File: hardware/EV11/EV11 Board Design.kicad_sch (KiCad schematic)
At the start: 141 parts, among them CN2 Conn_05x02_Female, CN3 Conn_01x06_Female, CN4 Conn_01x06_Female, CN5 Conn_02x05_Male, CN6 Conn_02x05_Male, CN7 Conn_02x05_Male, J1 Conn_01x02_Socket, J10 Conn_01x08_Socket, J2 AudioJack1, J3 Conn_01x06_Socket, J9 USB_C_Receptacle, SW1 TS-1037-A11B3-D2, SW3 TS-1037-A11B3-D2, SW4 SW_Push, SW5 SW_Push, SW6 SW_SPDT, U1 STM32F405RGTx, U11 ESP32-S3-WROOM-1-N8R2, U13 BM14B(0.8)-24DS-0.4V(53), U2 BQ21040DBV, U3 CH340C, U4 USBLC6-2P6, U5 M24C02-RMN6TP, U6 WM8960CGEFL/RV, U7 TPS63060, U8 STM32F070CBTx, U9 WM8960CGEFL/RV, Y1 Crystal_GND24

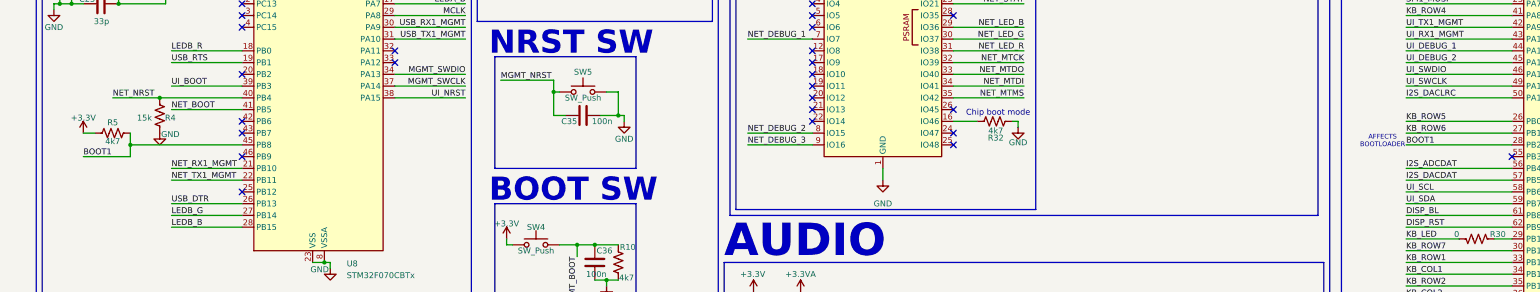
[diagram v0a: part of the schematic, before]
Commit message: Added larger courtyard to the keyboard connector to match the physical connector
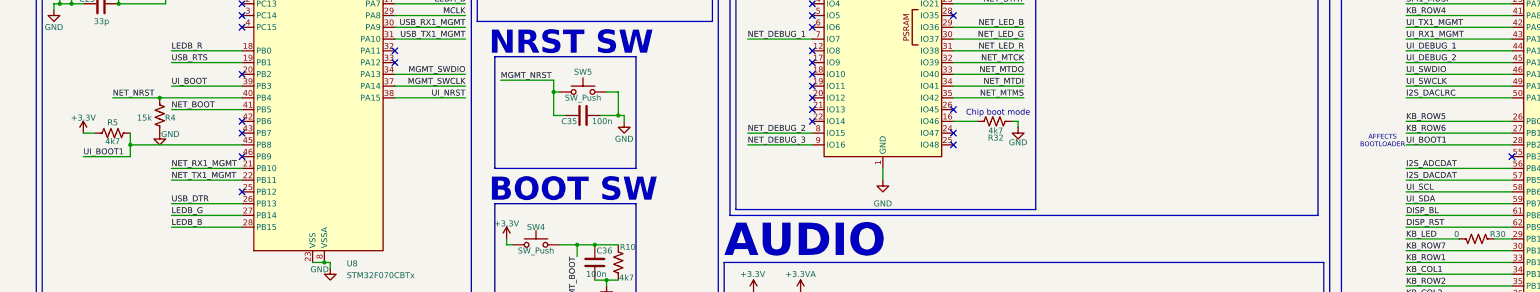
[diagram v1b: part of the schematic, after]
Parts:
- U13: footprint BM14B(0.B)-24DS-0:BM14B(0.B)-24DS-0.4V(53) -> Hactar_Footprints:BM14B(0.B)-24DS-0.4V(53)
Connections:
- net BOOT1 renamed UI_BOOT1
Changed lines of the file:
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@@
 		)
 	)
-	(label "BOOT1"
+	(label "UI_BOOT1"
 		(at 325.12 142.24 0)
 		(fields_autoplaced yes)
@@
 		)
 	)
-	(label "BOOT1"
+	(label "UI_BOOT1"
 		(at 39.37 144.78 0)
 		(fields_autoplaced yes)
@@
 			)
 		)
-		(property "Footprint" "BM14B(0.B)-24DS-0:BM14B(0.B)-24DS-0.4V(53)"
+		(property "Footprint" "Hactar_Footprints:BM14B(0.B)-24DS-0.4V(53)"
 			(at 355.6 306.07 0)
 			(effects

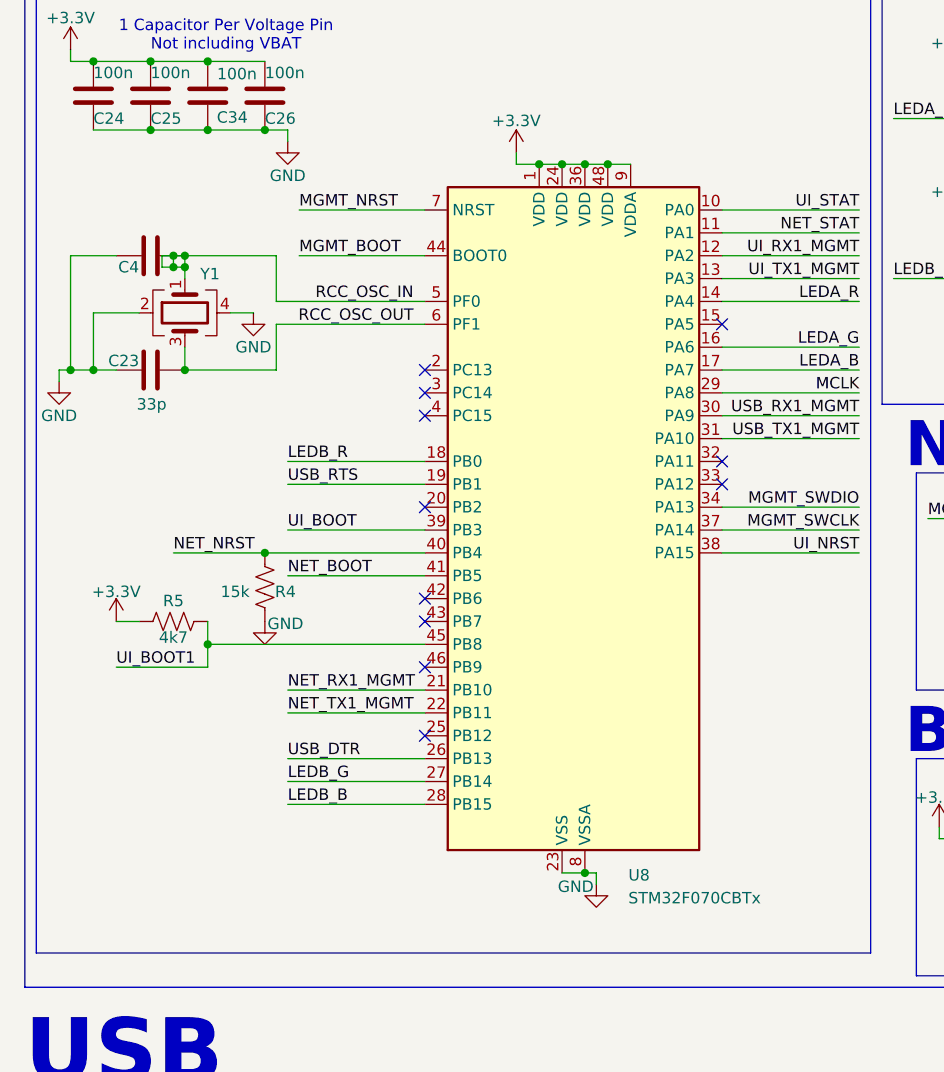
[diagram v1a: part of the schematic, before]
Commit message: Fix jlcpcb attributes
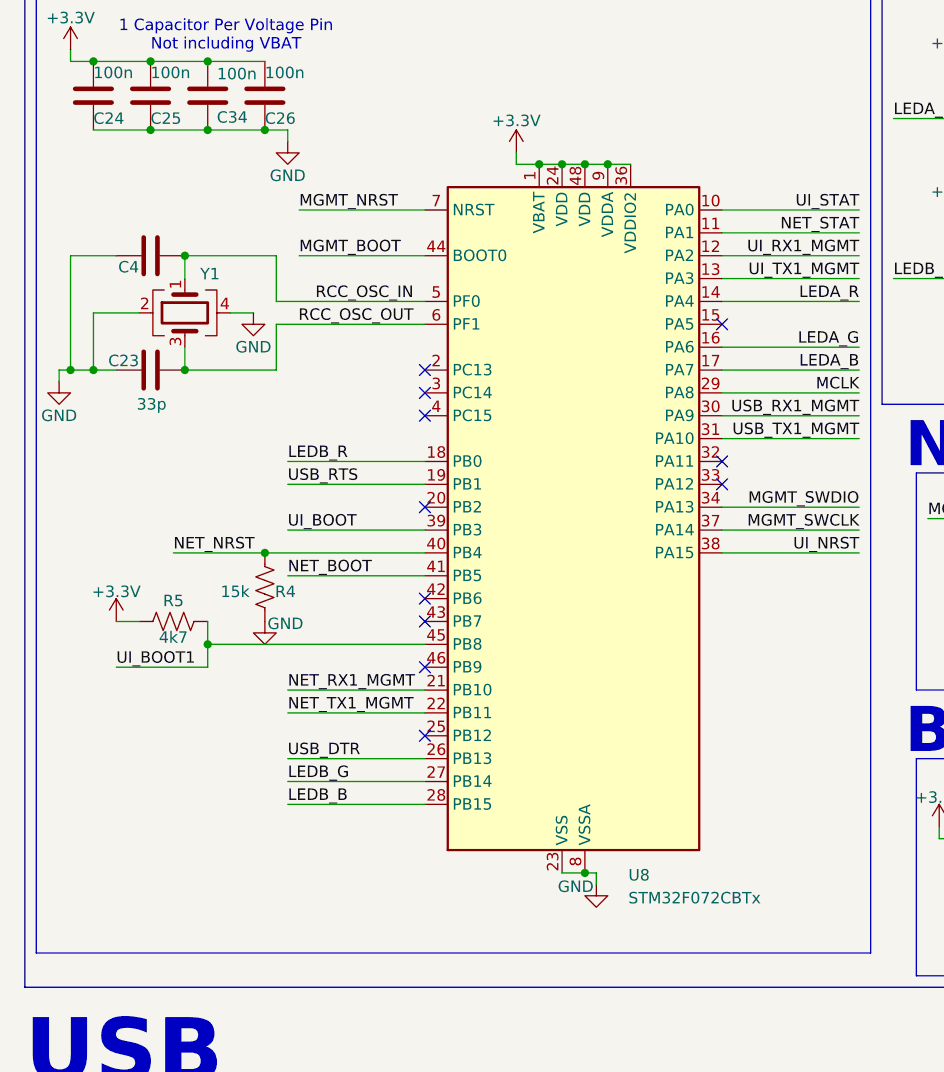
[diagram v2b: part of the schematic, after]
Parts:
- J2: JLCPCB Position Offset (none) -> 0.889,0; JLCPCB Rotation Offset (none) -> 90; MPN (none) -> PJ-320D
- TP1, TP2: now left out of the parts list
- U11: JLCPCB Position Offset 0,-0.254 -> 0,-0.508
- U13: JLCPCB Position Offset 2.2225,0.889 -> 2.9800,1.2065
- U6: JLCPCB Rotation Offset (none) -> -90
- U8: value STM32F070CBTx -> STM32F072CBTx; symbol MCU_ST_STM32F0:STM32F070CBTx -> MCU_ST_STM32F0:STM32F072C8Tx; JLCPCB Part # (none) -> C80488
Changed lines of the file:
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@@
 	)
 	(junction
-		(at 46.99 100.33)
-		(diameter 0)
-		(color 0 0 0 0)
-	)
-	(junction
 		(at 257.81 322.58)
 		(diameter 0)
@@
 	)
 	(junction
-		(at 45.72 99.06)
-		(diameter 0)
-		(color 0 0 0 0)
-	)
-	(junction
-		(at 45.72 100.33)
-		(diameter 0)
-		(color 0 0 0 0)
-	)
-	(junction
 		(at 196.85 351.79)
 		(diameter 0)
@@
 		)
 	)
-	(wire
-		(pts
-			(xy 45.72 99.06) (xy 45.72 100.33)
-		)
-		(stroke
-			(width 0)
-			(type default)
-		)
-	)
 	(polyline
 		(pts
@@
 	(wire
 		(pts
-			(xy 45.72 99.06) (xy 44.45 99.06)
-		)
-		(stroke
-			(width 0)
-			(type default)
-		)
-	)
-	(wire
-		(pts
 			(xy 57.15 217.17) (xy 57.15 219.71)
 		)
@@
 	(wire
 		(pts
-			(xy 44.45 99.06) (xy 44.45 100.33)
-		)
-		(stroke
-			(width 0)
-			(type default)
-		)
-	)
-	(wire
-		(pts
 			(xy 265.43 351.79) (xy 267.97 351.79)
 		)
@@
 	(wire
 		(pts
-			(xy 46.99 100.33) (xy 46.99 101.6)
-		)
-		(stroke
-			(width 0)
-			(type default)
-		)
-	)
-	(wire
-		(pts
 			(xy 134.62 351.79) (xy 142.24 351.79)
 		)
@@
 	(wire
 		(pts
-			(xy 46.99 99.06) (xy 45.72 99.06)
-		)
-		(stroke
-			(width 0)
-			(type default)
-		)
-	)
-	(wire
-		(pts
 			(xy 173.99 101.6) (xy 167.64 101.6)
 		)
@@
 	(wire
 		(pts
-			(xy 46.99 99.06) (xy 46.99 100.33)
+			(xy 46.99 99.06) (xy 46.99 101.6)
 		)
 		(stroke
@@
 	(wire
 		(pts
-			(xy 44.45 100.33) (xy 45.72 100.33)
-		)
-		(stroke
-			(width 0)
-			(type default)
-		)
-	)
-	(wire
-		(pts
 			(xy 279.4 223.52) (xy 283.21 223.52)
 		)
@@
 		)
 	)
-	(wire
-		(pts
-			(xy 46.99 100.33) (xy 45.72 100.33)
-		)
-		(stroke
-			(width 0)
-			(type default)
-		)
-	)
 	(polyline
 		(pts
@@
 			)
 		)
+		(property "JLCPCB Rotation Offset" "-90"
+			(at 231.14 248.92 0)
+			(effects
+				(font
+					(size 1.27 1.27)
+				)
+				(hide yes)
+			)
+		)
 		(pin "1"
 		)
@@
 			)
 		)
-		(property "JLCPCB Position Offset" "2.2225,0.889"
+		(property "JLCPCB Position Offset" "2.9800,1.2065"
 			(at 351.79 300.99 0)
 			(effects
@@
 	)
 	(symbol
-		(lib_id "MCU_ST_STM32F0:STM32F070CBTx")
+		(lib_id "MCU_ST_STM32F0:STM32F072C8Tx")
 		(at 88.9 129.54 0)
 		(unit 1)
@@
 			)
 		)
-		(property "Value" "STM32F070CBTx"
+		(property "Value" "STM32F072CBTx"
 			(at 96.266 170.434 0)
 			(effects
@@
 			)
 		)
-		(property "Datasheet" "https://www.st.com/resource/en/datasheet/stm32f070cb.pdf"
+		(property "Datasheet" "https://www.st.com/resource/en/datasheet/stm32f072c8.pdf"
+			(at 88.9 129.54 0)
+			(effects
+				(font
+					(size 1.27 1.27)
+				)
+				(hide yes)
+			)
+		)
+		(property "Description" "STMicroelectronics Arm Cortex-M0 MCU, 64KB flash, 16KB RAM, 48 MHz, 2.0-3.6V, 37 GPIO, LQFP48"
 			(at 88.9 129.54 0)
 			(effects
@@
 			)
 		)
-		(property "Description" "STMicroelectronics Arm Cortex-M0 MCU, 128KB flash, 16KB RAM, 48 MHz, 2.4-3.6V, 37 GPIO, LQFP48"
+		(property "JLCPCB Part #" "C80488"
 			(at 88.9 129.54 0)
 			(effects
@@
 			)
 		)
+		(property "MPN" "PJ-320D"
+			(at 359.41 222.25 0)
+			(effects
+				(font
+					(size 1.27 1.27)
+				)
+				(hide yes)
+			)
+		)
+		(property "JLCPCB Rotation Offset" "90"
+			(at 359.41 222.25 0)
+			(effects
+				(font
+					(size 1.27 1.27)
+				)
+				(hide yes)
+			)
+		)
+		(property "JLCPCB Position Offset" "0.889,0"
+			(at 359.41 222.25 0)
+			(effects
+				(font
+					(size 1.27 1.27)
+				)
+				(hide yes)
+			)
+		)
 		(pin "R1"
 		)
@@
 		(unit 1)
 		(exclude_from_sim no)
-		(in_bom yes)
+		(in_bom no)
 		(on_board yes)
 		(dnp no)
@@
 			)
 		)
-		(property "JLCPCB Position Offset" "0,-0.254"
+		(property "JLCPCB Position Offset" "0,-0.508"
 			(at 212.09 119.38 0)
 			(effects
@@
 		(unit 1)
 		(exclude_from_sim no)
-		(in_bom yes)
+		(in_bom no)
 		(on_board yes)
 		(dnp no)

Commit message: Clean up traces, add missing 3d models
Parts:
- removed C21, C22, C27: 100n, Capacitor_SMD:C_0402_1005Metric, symbol Device:C
- removed C33, C52: 4u7, Capacitor_SMD:C_0402_1005Metric, symbol Device:C
- removed C49, C50: 1u, Capacitor_SMD:C_0402_1005Metric, symbol Device:C
- removed C51, C55: 4.7u, Capacitor_SMD:C_0402_1005Metric, symbol Device:C
- removed C53, C54: 100u, Capacitor_SMD:C_1206_3216Metric, symbol Device:C
- removed JP2: SolderJumper_2_Bridged, NetTie:NetTie-2_SMD_Pad0.5mm, symbol Jumper:SolderJumper_2_Bridged
- removed R43: 2k2, Resistor_SMD:R_0402_1005Metric, symbol Device:R_US
- removed U9: WM8960CGEFL/RV, Package_DFN_QFN:QFN-32-1EP_5x5mm_P0.5mm_EP3.45x3.45mm_ThermalVias, symbol Hactar_Symbols:WM8960CGEFL/RV_1
- added JP3: SolderJumper_2_Bridged, Jumper:SolderJumper-2_P1.3mm_Bridged_RoundedPad1.0x1.5mm, symbol Jumper:SolderJumper_2_Bridged
- CN3, CN4, J3: footprint Connector_JST:JST_SHL_SM06B-SHLS-TF_1x06-1MP_P1.00mm_Horizontal -> Connector_JST:JST_SH_BM06B-SRSS-TB_1x06-1MP_P1.00mm_Vertical
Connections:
- net +3.3V: now also JP3.2 (B); no longer U3.4 (V3)
- net KB_MIC: no longer U6.5 (RINPUT1)
- net MGMT_BOOT: now also CN3.5 (Pin_5); no longer CN3.2 (Pin_2)
- net MGMT_NRST: now also CN3.4 (Pin_4); no longer CN3.3 (Pin_3)
- net MGMT_SWCLK: now also CN3.2 (Pin_2); no longer CN3.5 (Pin_5)
- net MGMT_SWDIO: now also CN3.3 (Pin_3); no longer CN3.4 (Pin_4)
- net NET_BOOT: now also J3.2 (Pin_2); no longer J3.5 (Pin_5)
- net NET_NRST: now also J3.5 (Pin_5); no longer J3.2 (Pin_2)
- net NET_RX1_MGMT: now also J3.4 (Pin_4); no longer J3.3 (Pin_3)
- net NET_TX1_MGMT: now also J3.3 (Pin_3); no longer J3.4 (Pin_4)
- net UI_BOOT: now also CN4.5 (Pin_5); no longer CN4.2 (Pin_2)
- net UI_NRST: now also CN4.4 (Pin_4); no longer CN4.3 (Pin_3)
- net UI_SWCLK: now also CN4.2 (Pin_2); no longer CN4.5 (Pin_5)
- net UI_SWDIO: now also CN4.3 (Pin_3); no longer CN4.4 (Pin_4)
- new net: JP3.1 (A), U3.4 (V3)
- no-connect marks 68 -> 60
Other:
- note removed: "JUST HERE FOR REVIEW"

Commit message: Update ev11 to use vertical 6pin jst connectors
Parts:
- CN3, CN4: JLCPCB Part # C3029345 -> C3029336; JLCPCB# C3029345 -> (none)
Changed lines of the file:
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@@
 			)
 		)
-		(property "JLCPCB Part #" "C3029345"
+		(property "JLCPCB Part #" "C3029336"
 			(at 420.37 259.08 0)
 			(effects
@@
 			)
 		)
-		(property "JLCPCB#" "C3029345"
-			(at 420.37 280.67 0)
-			(effects
-				(font
-					(size 1.27 1.27)
-				)
-				(hide yes)
-			)
-		)
 		(pin "3"
 		)
@@
 			)
 		)
-		(property "JLCPCB Part #" "C3029345"
+		(property "JLCPCB Part #" "C3029336"
 			(at 420.37 224.79 0)
 			(effects
 				(font
-					(size 1.27 1.27)
-				)
-				(hide yes)
-			)
-		)
-		(property "JLCPCB#" "C3029345"
-			(at 420.37 246.38 0)
-			(effects
-				(font

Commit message: Fix rotation problem for 6 pin jst connectors
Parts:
- CN3, CN4, J3: JLCPCB Rotation Offset (none) -> 180
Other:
- note added: "GPIO Debug"
- note added: "I2S & I2C Debug"
- note added: "NET Serial Uploader"
- note added: "Serial Debug"
- moved on the sheet: R36, R37, R38, R39, R40, R41, R7, R8

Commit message: Update ev11 to have missing 3d models, remove old wm8960 schematic
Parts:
- SW6: footprint Button_Switch_THT:SW_E-Switch_EG1224_SPDT_Angled -> Hactar_Footprints:SW-TH_SS-12D11G5R; JLCPCB Part # C273395 -> C388633; JLCPCB Position Offset 0.1, 4.1 -> 0,-3.556
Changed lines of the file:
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@@
 			)
 		)
-		(property "Footprint" "Button_Switch_THT:SW_E-Switch_EG1224_SPDT_Angled"
+		(property "Footprint" "Hactar_Footprints:SW-TH_SS-12D11G5R"
 			(at 96.52 311.15 0)
 			(effects
@@
 			)
 		)
-		(property "JLCPCB Part #" "C273395"
+		(property "JLCPCB Part #" "C388633"
 			(at 96.52 311.15 0)
 			(effects
@@
 			)
 		)
-		(property "JLCPCB Position Offset" "0.1, 4.1"
+		(property "JLCPCB Position Offset" "0,-3.556"
 			(at 96.52 311.15 0)
 			(effects

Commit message: Added missing jlcpcb part number
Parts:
- R42: JLCPCB Part # (none) -> C111027
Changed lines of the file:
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@@
 			)
 		)
-		(property "JLCPCB Part #" ""
+		(property "JLCPCB Part #" "C111027"
 			(at 120.65 322.58 0)
 			(effects
